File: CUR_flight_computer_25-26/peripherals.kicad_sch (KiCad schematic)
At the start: 17 parts, among them J13 Conn_01x04_Pin, Q1 NTR4003N, SW3 GSPTS0018, SW4 GSPTS0018, SW5 GSPTS0018

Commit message: added mosfet for buzszer
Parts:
- Q1: footprint Resistor_SMD:R_0603_1608Metric -> NTR4003NT1G:SOT96P237X111-3N
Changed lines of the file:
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@@
 			)
 		)
-		(property "Footprint" "Resistor_SMD:R_0603_1608Metric"
+		(property "Footprint" "NTR4003NT1G:SOT96P237X111-3N"
 			(at 53.34 58.42 0)
 			(effects

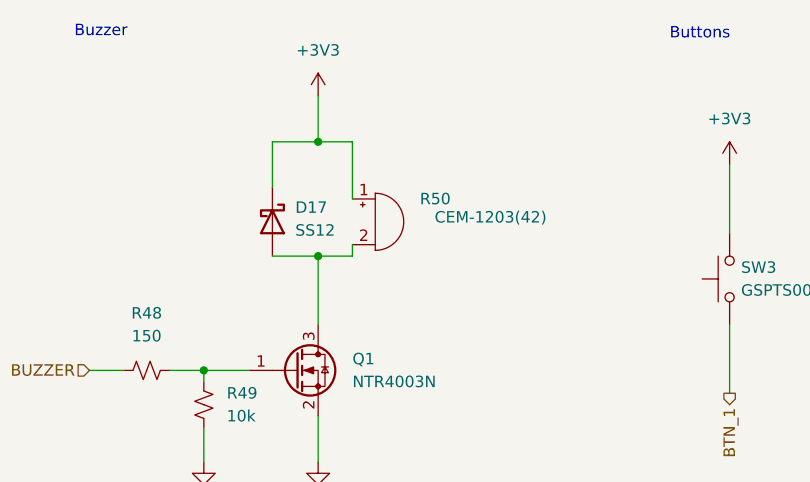
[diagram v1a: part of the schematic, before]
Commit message: cahnged buzzer
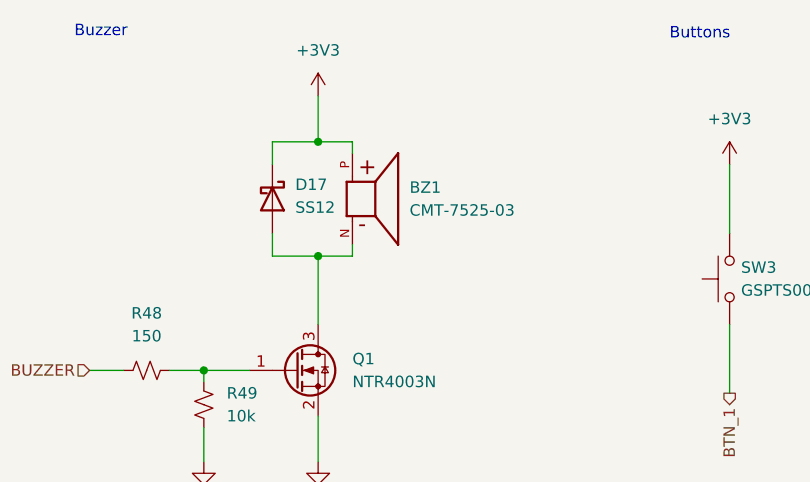
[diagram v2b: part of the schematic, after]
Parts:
- removed R50: CEM-1203(42), Buzzer_SameSky:Buzzer_SameSky_CEM-1203_42, symbol Device:Buzzer
- added BZ1: CMT-7525-03, CMT-7525-03-SMT-TR:XDCR_CMT-7525-03-SMT-TR, symbol CMT-7525-03-SMT-TR:CMT-7525-03-SMT-TR
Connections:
- net +3V3: now also BZ1.P
- net at D17.2 (A), Q1.3 (D): now also BZ1.N
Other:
- moved on the sheet: D17
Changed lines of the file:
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@@
 	(wire
 		(pts
-			(xy 45.72 35.56) (xy 45.72 40.64)
+			(xy 45.72 35.56) (xy 45.72 38.1)
 		)
 		(stroke
@@
 	(wire
 		(pts
+			(xy 45.72 48.26) (xy 45.72 45.72)
+		)
+		(stroke
+			(width 0)
+			(type default)
+		)
+	)
+	(wire
+		(pts
 			(xy 45.72 48.26) (xy 50.8 48.26)
 		)
@@
 	(wire
 		(pts
-			(xy 54.61 41.91) (xy 54.61 35.56)
-		)
-		(stroke
-			(width 0)
-			(type default)
-		)
-	)
-	(wire
-		(pts
 			(xy 72.39 129.54) (xy 72.39 125.73)
 		)
@@
 		(pts
 			(xy 115.57 55.88) (xy 115.57 63.5)
+		)
+		(stroke
+			(width 0)
+			(type default)
+		)
+	)
+	(wire
+		(pts
+			(xy 54.61 36.83) (xy 54.61 35.56)
 		)
 		(stroke
@@
 	)
 	(symbol
-		(lib_id "Device:Buzzer")
-		(at 57.15 44.45 0)
-		(unit 1)
-		(exclude_from_sim no)
-		(in_bom yes)
-		(on_board yes)
-		(dnp no)
-		(property "Reference" "R50"
-			(at 65.532 41.91 0)
-			(effects
-				(font
-					(size 1.27 1.27)
-				)
-				(justify right)
-			)
-		)
-		(property "Value" "CEM-1203(42)"
-			(at 76.2 43.942 0)
-			(effects
-				(font
-					(size 1.27 1.27)
-				)
-				(justify right)
-			)
-		)
-		(property "Footprint" "Buzzer_SameSky:Buzzer_SameSky_CEM-1203_42"
-			(at 109.22 132.08 0)
-			(effects
-				(font
-					(size 1.27 1.27)
-				)
-				(hide yes)
-			)
-		)
-		(property "Datasheet" "~"
-			(at 109.22 132.08 0)
-			(effects
-				(font
-					(size 1.27 1.27)
-				)
-				(hide yes)
-			)
-		)
-		(property "Description" "Resistor, small US symbol"
-			(at 109.22 132.08 0)
-			(effects
-				(font
-					(size 1.27 1.27)
-				)
-				(hide yes)
-			)
-		)
-		(pin "1"
-		)
-		(pin "2"
-		)
-		(instances
-			(project "CUR_flight_computer_25-26"
-				(path "/bf7761cc-1b32-4d86-809c-5f027005229b/5946e354-b9a7-4a8a-8580-991442920c21"
-					(reference "R50")
-					(unit 1)
-				)
-			)
-		)
-	)
-	(symbol
 		(lib_id "Diode:SS12")
-		(at 45.72 44.45 270)
+		(at 45.72 41.91 270)
 		(unit 1)
 		(exclude_from_sim no)
@@
 		(fields_autoplaced yes)
 		(property "Reference" "D17"
+			(at 48.26 40.3224 90)
+			(effects
+				(font
+					(size 1.27 1.27)
+				)
+				(justify left)
+			)
+		)
+		(property "Value" "SS12"
 			(at 48.26 42.8624 90)
 			(effects
@@
 			)
 		)
-		(property "Value" "SS12"
-			(at 48.26 45.4024 90)
-			(effects
-				(font
-					(size 1.27 1.27)
-				)
-				(justify left)
-			)
-		)
 		(property "Footprint" "Diode_SMD:D_SMA"
-			(at 41.275 44.45 0)
+			(at 41.275 41.91 0)
 			(effects
 				(font
@@
 		)
 		(property "Datasheet" "https://www.vishay.com/docs/88746/ss12.pdf"
-			(at 45.72 44.45 0)
+			(at 45.72 41.91 0)
 			(effects
 				(font
@@
 		)
 		(property "Description" "20V 1A Schottky Diode, SMA"
-			(at 45.72 44.45 0)
+			(at 45.72 41.91 0)
 			(effects
 				(font
@@
 					(unit 1)
 				)
+			)
+		)
+	)
+	(symbol
+		(lib_id "CMT-7525-03-SMT-TR:CMT-7525-03-SMT-TR")
+		(at 57.15 41.91 0)
+		(unit 1)
+		(exclude_from_sim no)
+		(in_bom yes)
+		(on_board yes)
+		(dnp no)
+		(fields_autoplaced yes)
+		(property "Reference" "BZ1"
+			(at 60.96 40.6399 0)
+			(effects
+				(font
+					(size 1.27 1.27)
+				)
+				(justify left)
+			)
+		)
+		(property "Value" "CMT-7525-03"
+			(at 60.96 43.1799 0)
+			(effects
+				(font
+					(size 1.27 1.27)
+				)
+				(justify left)
+			)
+		)
+		(property "Footprint" "CMT-7525-03-SMT-TR:XDCR_CMT-7525-03-SMT-TR"
+			(at 57.15 41.91 0)
+			(effects
+				(font
+					(size 1.27 1.27)
+				)
+				(justify bottom)
+				(hide yes)
+			)
+		)
+		(property "Datasheet" ""
+			(at 57.15 41.91 0)
+			(effects
+				(font
+					(size 1.27 1.27)
+				)
+				(hide yes)
+			)
+		)
+		(property "Description" ""
+			(at 57.15 41.91 0)
+			(effects
+				(font
+					(size 1.27 1.27)
+				)
+				(hide yes)
+			)
+		)
+		(property "PARTREV" "1.0"
+			(at 57.15 41.91 0)
+			(effects
+				(font
+					(size 1.27 1.27)
+				)
+				(justify bottom)
+				(hide yes)
+			)
+		)
+		(property "STANDARD" "Manufacturer Recommendations"
+			(at 57.15 41.91 0)
+			(effects
+				(font
+					(size 1.27 1.27)
+				)
+				(justify bottom)
+				(hide yes)
+			)
+		)
+		(property "MAXIMUM_PACKAGE_HEIGHT" "2.7mm"
+			(at 57.15 41.91 0)
+			(effects
+				(font
+					(size 1.27 1.27)
+				)
+				(justify bottom)
+				(hide yes)
+			)
+		)
+		(property "MANUFACTURER" "Same Sky"
+			(at 57.15 41.91 0)
+			(effects
+				(font
+					(size 1.27 1.27)
+				)
+				(justify bottom)
+				(hide yes)
+			)
+		)
+		(pin "N"
+		)
+		(pin "P"
+		)
+		(instances
+			(project ""
+				(path "/bf7761cc-1b32-4d86-809c-5f027005229b/5946e354-b9a7-4a8a-8580-991442920c21"
+					(reference "BZ1")
+					(unit 1)
+				)

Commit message: updated buzzer
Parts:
- BZ1: footprint CMT-7525-03-SMT-TR:XDCR_CMT-7525-03-SMT-TR -> Buzzer_SameSky:XDCR_CMT-7525-03-SMT-TR
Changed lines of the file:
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@@
 			)
 		)
-		(property "Footprint" "CMT-7525-03-SMT-TR:XDCR_CMT-7525-03-SMT-TR"
+		(property "Footprint" "Buzzer_SameSky:XDCR_CMT-7525-03-SMT-TR"
 			(at 57.15 41.91 0)
 			(effects

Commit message: more layout yay
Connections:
- net +3V3: now also BZ1.1; no longer BZ1.P
- net at D17.2 (A), Q1.3 (D): now also BZ1.2; no longer BZ1.N
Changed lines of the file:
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@@
 			)
 		)
-		(pin "N"
+		(pin "2"
 		)
-		(pin "P"
+		(pin "1"
 		)
 		(instances

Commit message: Layout groups
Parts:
- removed D17: SS12, Diode_SMD:D_SMA, symbol Diode:SS12
- added D3: BAT54-7-F, Package_TO_SOT_SMD:SOT-23, symbol Diode:BAT54C
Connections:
- net +3V3: now also D3.3
- net at BZ1.2, Q1.3 (D): now also D3.1
- no-connect marks 0 -> 1
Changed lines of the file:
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@@
 		(color 0 0 0 0)
 	)
+	(no_connect
+		(at 33.02 48.26)
+	)
 	(wire
 		(pts
@@
 	(wire
 		(pts
-			(xy 45.72 35.56) (xy 45.72 38.1)
-		)
-		(stroke
-			(width 0)
-			(type default)
-		)
-	)
-	(wire
-		(pts
 			(xy 50.8 48.26) (xy 50.8 55.88)
 		)
@@
 	(wire
 		(pts
-			(xy 45.72 48.26) (xy 45.72 45.72)
-		)
-		(stroke
-			(width 0)
-			(type default)
-		)
-	)
-	(wire
-		(pts
-			(xy 45.72 48.26) (xy 50.8 48.26)
+			(xy 48.26 48.26) (xy 50.8 48.26)
 		)
 		(stroke
@@
 	(wire
 		(pts
-			(xy 50.8 35.56) (xy 45.72 35.56)
+			(xy 40.64 35.56) (xy 50.8 35.56)
 		)
 		(stroke
@@
 		(pts
 			(xy 107.95 118.11) (xy 107.95 114.3)
+		)
+		(stroke
+			(width 0)
+			(type default)
+		)
+	)
+	(wire
+		(pts
+			(xy 40.64 43.18) (xy 40.64 35.56)
 		)
 		(stroke
@@
 				(path "/bf7761cc-1b32-4d86-809c-5f027005229b/5946e354-b9a7-4a8a-8580-991442920c21"
 					(reference "#PWR0110")
-					(unit 1)
-				)
-			)
-		)
-	)
-	(symbol
-		(lib_id "Diode:SS12")
-		(at 45.72 41.91 270)
-		(unit 1)
-		(exclude_from_sim no)
-		(in_bom yes)
-		(on_board yes)
-		(dnp no)
-		(fields_autoplaced yes)
-		(property "Reference" "D17"
-			(at 48.26 40.3224 90)
-			(effects
-				(font
-					(size 1.27 1.27)
-				)
-				(justify left)
-			)
-		)
-		(property "Value" "SS12"
-			(at 48.26 42.8624 90)
-			(effects
-				(font
-					(size 1.27 1.27)
-				)
-				(justify left)
-			)
-		)
-		(property "Footprint" "Diode_SMD:D_SMA"
-			(at 41.275 41.91 0)
-			(effects
-				(font
-					(size 1.27 1.27)
-				)
-				(hide yes)
-			)
-		)
-		(property "Datasheet" "https://www.vishay.com/docs/88746/ss12.pdf"
-			(at 45.72 41.91 0)
-			(effects
-				(font
-					(size 1.27 1.27)
-				)
-				(hide yes)
-			)
-		)
-		(property "Description" "20V 1A Schottky Diode, SMA"
-			(at 45.72 41.91 0)
-			(effects
-				(font
-					(size 1.27 1.27)
-				)
-				(hide yes)
-			)
-		)
-		(pin "1"
-		)
-		(pin "2"
-		)
-		(instances
-			(project ""
-				(path "/bf7761cc-1b32-4d86-809c-5f027005229b/5946e354-b9a7-4a8a-8580-991442920c21"
-					(reference "D17")
 					(unit 1)
 				)
@@
 					(unit 1)
 				)
+			)
+		)
+	)
+	(symbol
+		(lib_id "Diode:BAT54C")
+		(at 40.64 48.26 180)
+		(unit 1)
+		(exclude_from_sim no)
+		(in_bom yes)
+		(on_board yes)
+		(dnp no)
+		(fields_autoplaced yes)
+		(property "Reference" "D3"
+			(at 40.64 52.07 0)
+			(effects
+				(font
+					(size 1.27 1.27)
+				)
+			)
+		)
+		(property "Value" "BAT54-7-F"
+			(at 40.64 54.61 0)
+			(effects
+				(font
+					(size 1.27 1.27)
+				)
+			)
+		)
+		(property "Footprint" "Package_TO_SOT_SMD:SOT-23"
+			(at 38.735 51.435 0)
+			(effects
+				(font
+					(size 1.27 1.27)
+				)
+				(justify left)
+				(hide yes)
+			)
+		)
+		(property "Datasheet" "http://www.diodes.com/_files/datasheets/ds11005.pdf"
+			(at 42.672 48.26 0)
+			(effects
+				(font
+					(size 1.27 1.27)
+				)
+				(hide yes)
+			)
+		)
+		(property "Description" "dual schottky barrier diode, common cathode"
+			(at 40.64 48.26 0)
+			(effects
+				(font
+					(size 1.27 1.27)
+				)
+				(hide yes)
+			)
+		)
+		(pin "3"
+		)
+		(pin "2"
+		)
+		(pin "1"
+		)
+		(instances
+			(project ""
+				(path "/bf7761cc-1b32-4d86-809c-5f027005229b/5946e354-b9a7-4a8a-8580-991442920c21"
+					(reference "D3")
+					(unit 1)
+				)

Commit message: Fix NTR4003N footprint
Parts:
- Q1: footprint NTR4003NT1G:SOT96P237X111-3N -> Package_TO_SOT_SMD:SOT-23
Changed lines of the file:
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@@
 			)
 		)
-		(property "Footprint" "NTR4003NT1G:SOT96P237X111-3N"
+		(property "Footprint" "Package_TO_SOT_SMD:SOT-23"
 			(at 53.34 58.42 0)
 			(effects
@@
 			)
 		)
-		(property "Sim.Library" "kicad-library-sigmondkukla\\spice\\NTR4003N.LIB"
+		(property "Sim.Library" "kicad-library\\spice\\NTR4003N.LIB"
 			(at 48.26 60.96 0)
 			(effects

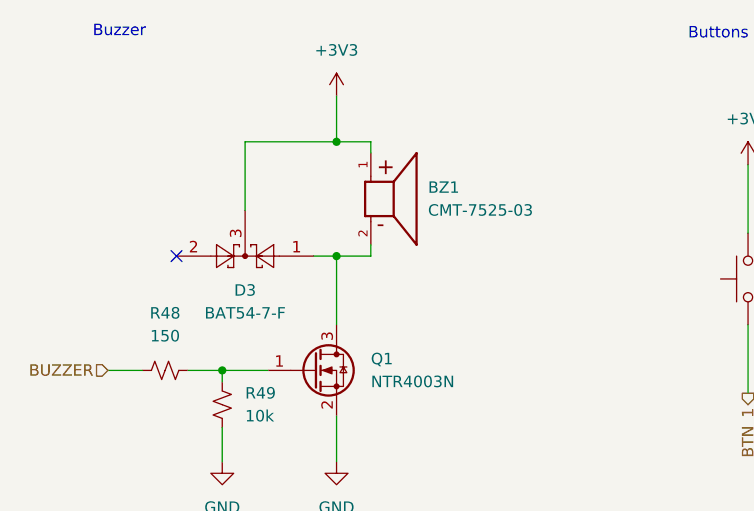
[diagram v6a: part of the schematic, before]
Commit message: Apply MPNs for capacitors and connectors
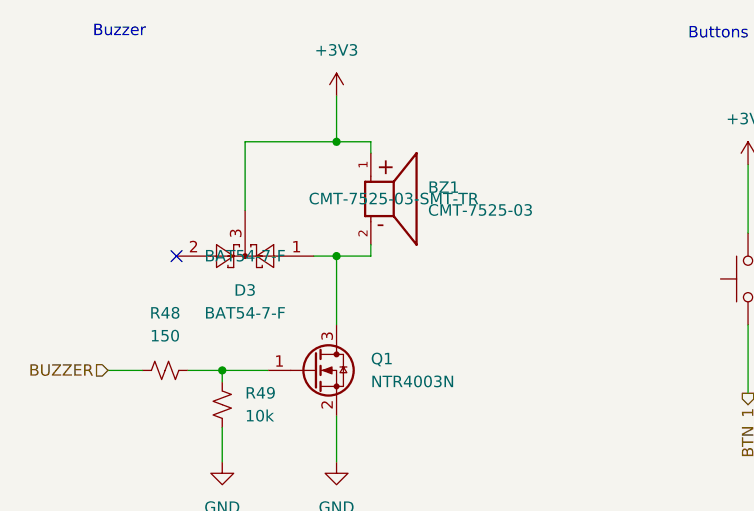
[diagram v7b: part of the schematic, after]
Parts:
- BZ1: MPN (none) -> CMT-7525-03-SMT-TR
- D3: MPN (none) -> BAT54-7-F
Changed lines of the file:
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@@
+			)
+		)
+		(property "MPN" "BAT54-7-F"
+			(at 40.64 48.26 0)
+			(effects
+				(font
+					(size 1.27 1.27)
+				)
 			)
 		)
@@
 			)
 		)
+		(property "MPN" "CMT-7525-03-SMT-TR"
+			(at 57.15 41.91 0)
+			(effects
+				(font
+					(size 1.27 1.27)
+				)
+			)
+		)

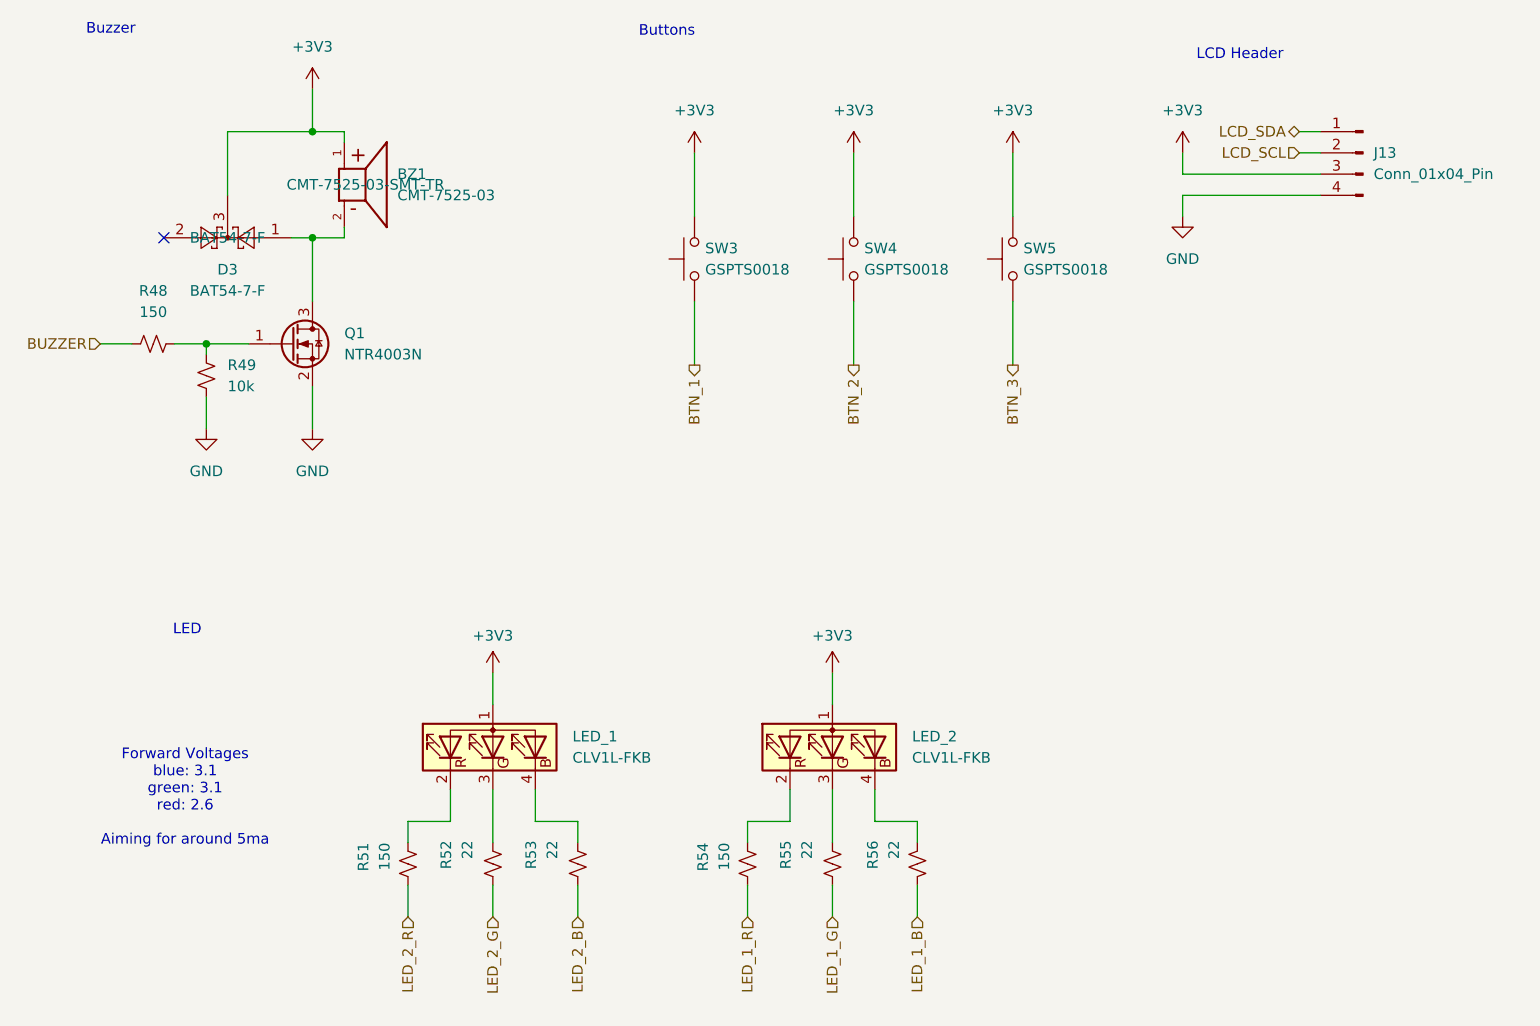
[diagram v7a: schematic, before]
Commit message: Add MPNs for ICs
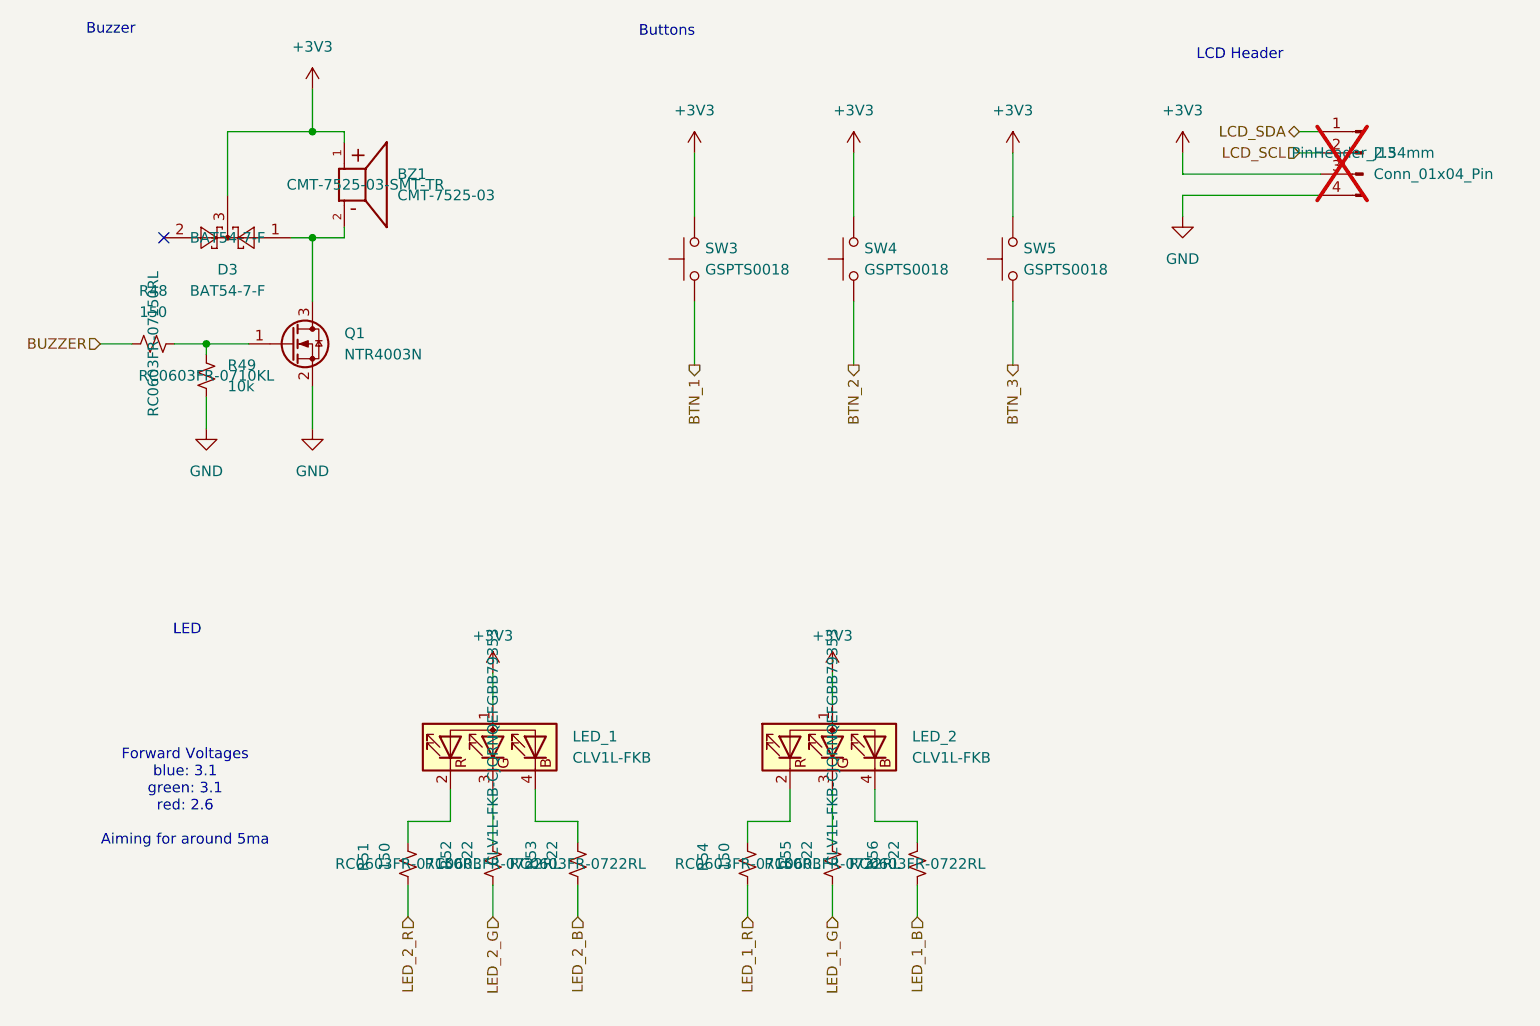
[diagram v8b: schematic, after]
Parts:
- J13: MPN (none) -> PinHeader_2.54mm; now not fitted; now left out of the parts list
- LED_1, LED_2: MPN (none) -> CLV1L-FKB-CJQRNQEFGBB79353
- R48, R51, R54: MPN (none) -> RC0603FR-07150RL
- R49: MPN (none) -> RC0603FR-0710KL
- R52, R53, R55, R56: MPN (none) -> RC0603FR-0722RL
- SW3, SW4, SW5: MPN SKRPADE010 -> PTS815SJG250SMTR LFS
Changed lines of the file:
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@@
+			)
+		)
+		(property "MPN" "RC0603FR-0722RL"
+			(at 72.39 123.19 0)
+			(effects
+				(font
+					(size 1.27 1.27)
+				)
 			)
 		)
@@
 				)
 				(hide yes)
+			)
+		)
+		(property "MPN" "CLV1L-FKB-CJQRNQEFGBB79353"
+			(at 72.39 109.22 0)
+			(effects
+				(font
+					(size 1.27 1.27)
+				)
 			)
 		)
@@
 		(unit 1)
 		(exclude_from_sim no)
-		(in_bom yes)
-		(on_board yes)
-		(dnp no)
+		(in_bom no)
+		(on_board yes)
+		(dnp yes)
 		(fields_autoplaced yes)
 		(property "Reference" "J13"
@@
 			)
 		)
+		(property "MPN" "PinHeader_2.54mm"
+			(at 176.53 38.1 0)
+			(effects
+				(font
+					(size 1.27 1.27)
+				)
+			)
+		)
 		(pin "3"
 		)
@@
 			)
 		)
+		(property "MPN" "CLV1L-FKB-CJQRNQEFGBB79353"
+			(at 113.03 109.22 0)
+			(effects
+				(font
+					(size 1.27 1.27)
+				)
+			)
+		)
 		(pin "2"
 		)
@@
 			)
 		)
+		(property "MPN" "RC0603FR-07150RL"
+			(at 62.23 123.19 0)
+			(effects
+				(font
+					(size 1.27 1.27)
+				)
+			)
+		)
 		(pin "1"
 		)
@@
 			)
 		)
+		(property "MPN" "RC0603FR-07150RL"
+			(at 102.87 123.19 0)
+			(effects
+				(font
+					(size 1.27 1.27)
+				)
+			)
+		)
 		(pin "1"
 		)
@@
 			)
 		)
+		(property "MPN" "RC0603FR-0722RL"
+			(at 113.03 123.19 0)
+			(effects
+				(font
+					(size 1.27 1.27)
+				)
+			)
+		)
 		(pin "1"
 		)
@@
 			)
 		)
-		(property "MPN" "SKRPADE010"
+		(property "MPN" "PTS815SJG250SMTR LFS"
 			(at 134.62 50.8 90)
 			(effects
@@
 			)
 		)
+		(property "MPN" "RC0603FR-0722RL"
+			(at 123.19 123.19 0)
+			(effects
+				(font
+					(size 1.27 1.27)
+				)
+			)
+		)
 		(pin "1"
 		)
@@
 			)
 		)
+		(property "MPN" "RC0603FR-0722RL"
+			(at 82.55 123.19 0)
+			(effects
+				(font
+					(size 1.27 1.27)
+				)
+			)
+		)
 		(pin "1"
 		)
@@
 			)
 		)
-		(property "MPN" "SKRPADE010"
+		(property "MPN" "PTS815SJG250SMTR LFS"
 			(at 115.57 50.8 90)
 			(effects
@@
 			)
 		)
-		(property "MPN" "SKRPADE010"
+		(property "MPN" "PTS815SJG250SMTR LFS"
 			(at 96.52 50.8 90)
 			(effects
@@
 			)
 		)
+		(property "MPN" "RC0603FR-0710KL"
+			(at 38.1 64.77 0)
+			(effects
+				(font
+					(size 1.27 1.27)
+				)
+			)
+		)
 		(pin "2"
 		)
@@
 			)
 		)
+		(property "MPN" "RC0603FR-07150RL"
+			(at 31.75 60.96 0)
+			(effects
+				(font
+					(size 1.27 1.27)
+				)
+			)
+		)
